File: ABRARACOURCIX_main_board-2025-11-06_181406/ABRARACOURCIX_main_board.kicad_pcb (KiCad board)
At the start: 2 copper layers, 140 x 140 mm, 72 parts, among them J1 Conn_01x02_Pin, J10 Conn_01x03_Socket, J11 Conn_01x03_Socket, J12 Conn_01x02_Pin, J2 XT60PW-M, J3 XT60PW-M, J4 Conn_01x06_Socket, J5 Conn_01x05_Socket, J6 Conn_01x03_Socket, J7 XT60PW-F, J8 Conn_01x03_Socket, J9 Conn_01x03_Socket, K1 Relai_T9GV1L14-5, Q2 NTR4101PT1G, Q3 MMBT3904, U2 Current_sens_ACS712ELCTR-20A-T, U3 AZ1117CH-3.3TRG1, U5 BNO055, U6 LMC6482, U7 LMC6482, U9 STM32F429VETx, Y2 ABS07-32.768KHZ-T

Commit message: Placement des composantes 95%
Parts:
- removed BUZ_D2: BAT54T1G, Diode_SMD:D_SOD-123
- removed BUZ_R3: 1k5, Resistor_SMD:R_1206_3216Metric_Pad1.30x1.75mm_HandSolder
- removed C12, C8, C9: 100n, Capacitor_SMD:C_1206_3216Metric_Pad1.33x1.80mm_HandSolder
- removed K1: Relai_T9GV1L14-5, Librairie_footprint:Relai_30A_T9GV1L14-5_TEC
- removed U9: STM32F429VETx, Package_QFP:LQFP-100_14x14mm_P0.5mm
- added Q5: DSS20200L-7-PNP, Package_TO_SOT_SMD:SOT-23-3, F.Cu at (-32.9, 6.80)
- added Q6: IKD15N60R, Package_TO_SOT_SMD:TO-252-2, F.Cu at (-45.1, 9.53)
- added R18: 1k5, Resistor_SMD:R_1206_3216Metric_Pad1.30x1.75mm_HandSolder, F.Cu at (-26.5, 12.0)
- added R19: 10k, Resistor_SMD:R_1206_3216Metric_Pad1.30x1.75mm_HandSolder, F.Cu at (-32.9, 2.20)
- added R2: 10k, Resistor_SMD:R_1206_3216Metric_Pad1.30x1.75mm_HandSolder, F.Cu at (-32.9, 12.0)
- added R20: 1k5, Resistor_SMD:R_1206_3216Metric_Pad1.30x1.75mm_HandSolder, F.Cu at (-26.5, 2.20)
- added U1: STM32F429VITx, Package_QFP:LQFP-100_14x14mm_P0.5mm, F.Cu at (13.5, -4.08)
- C27: footprint Capacitor_SMD:C_1206_3216Metric_Pad1.33x1.80mm_HandSolder -> Librairie_footprint:R60-CC_KEM
- Q3: value MMBT3904 -> NPN-DSS20201L-7; footprint Package_TO_SOT_SMD:SOT-23-3 -> Package_TO_SOT_SMD:SOT-23
- moved C27 187.4 mm to (-11.6, 32.9)
- moved C28 173.4 mm to (-39.2, 2.70)
- moved C29 173.1 mm to (-39.2, -1.10)
- moved DZ1 164.0 mm to (-29.2, -9.15)
- moved C19 161.8 mm to (-1.60, 6.40), turned to 90 degrees
- moved D2 157.0 mm to (6.35, 20.1), turned to -90 degrees
- moved C3 155.6 mm to (-20.2, 9.93), turned to -90 degrees
- moved J1 154.7 mm to (-21.9, -9.95)
- moved R17 153.4 mm to (10.8, 20.0), turned to -90 degrees
- moved J12 149.0 mm to (0.00, -61.0), turned to 90 degrees
- moved C4 148.3 mm to (5.70, -14.7)
- moved C5 145.6 mm to (2.20, 6.40), turned to 90 degrees
- moved TP6 143.9 mm to (46.2, -45.4)
- moved TP7 143.9 mm to (46.2, -41.3)
- moved C2 143.1 mm to (-6.80, 11.1), turned to 90 degrees
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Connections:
- J7 pad 1: GND -> Net-(J7-Pad1)
- J7 pad 2: VBAT -> Net-(U2-IP-)
- U2 pad 3: Net-(Q2-D) -> Net-(U2-IP-)
- U2 pad 4: Net-(Q2-D) -> Net-(U2-IP-)
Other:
- board text added: "3v3 Power"
- board text added: "5V GND"
- board text added: "Debug"
- board text added: "MTA Buck 5V In"
- board text added: "PWM 5V GND"

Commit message: Documentation de composantes
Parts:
- removed U6: LMC6482, Librairie_footprint:SOIC127P599X175-8N
- added GND1: TestPoint, TestPoint:TestPoint_THTPad_2.0x2.0mm_Drill1.0mm, F.Cu at (11.1, -36.3)
- added GND2: TestPoint, TestPoint:TestPoint_THTPad_2.0x2.0mm_Drill1.0mm, F.Cu at (15.8, 15.6)
- added U4: LMC6482AIMX/NOPB, Librairie_footprint:SOIC127P599X175-8N, F.Cu at (0.18, -44.8)
- C27: footprint Librairie_footprint:R60-CC_KEM -> Librairie_footprint:CAP_MU_15750_RUB-L
- R10: value 3K -> 1K
- R5: value 3K -> 1k
- U7: value LMC6482 -> LMC6482AIMX/NOPB
- moved C1 78.8 mm to (64.2, -8.40), turned to 90 degrees
- moved J12 78.4 mm to (58.1, -8.30), turned to 180 degrees
- moved SDA1 61.2 mm to (6.20, -25.8)
- moved RX1 60.6 mm to (25.8, 11.7)
- moved SCL1 55.3 mm to (11.1, -25.8)
- moved R5 55.3 mm to (13.0, -15.3)
- moved TX1 52.9 mm to (25.8, 7.50)
- moved R10 44.2 mm to (8.10, -19.7)
- moved C27 23.1 mm to (0.20, 13.0)
- moved J6 12.2 mm to (12.2, 56.0), turned to -90 degrees
- moved PWR_R5 11.9 mm to (-21.9, -4.60), turned to 0 degrees
- moved J10 8.89 mm to (2.64, 56.0)
- moved C3 8.67 mm to (-14.8, 3.14), turned to 90 degrees
- moved J2 7.40 mm to (-38.5, -9.20), turned to 180 degrees
- moved R8 3.67 mm to (-13.1, -11.3), turned to 0 degrees
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- renumbered TP6 to RX1, TP5 to SCL1, TP4 to SDA1, TP7 to TX1
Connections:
- net Net-(J2--) renamed /Power/20A_pre_switch
- J4 pad 2: +5V -> HC_RX
- J4 pad 3: GND -> HC_TX
- J4 pad 4: HC_TX -> GND
- J4 pad 5: HC_RX -> +5V
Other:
- board text added: "HC-05 Breakout"
- board text added: "Input 16v8 max"
- board text added: "Output to ESC"
- board text added: "PWM Moteur GND"
- board text added: "Projet ABRARACOURCIX V1 GAULxDesign IV 2025 Nathan Armishaw Étienne Bernier Marc-André Tremblay Rémi Plante Félix Dion"

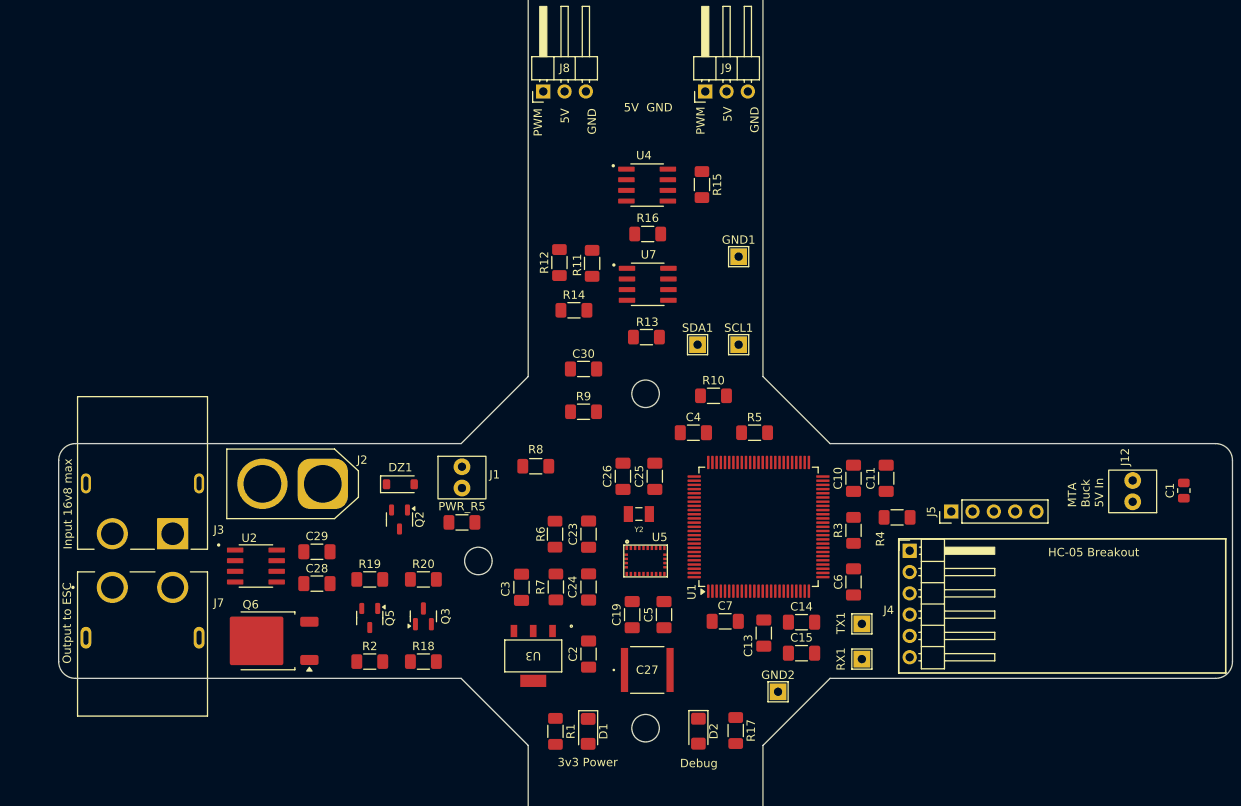
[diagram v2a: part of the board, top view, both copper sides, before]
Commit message: Déplacement des mounting holes et début du routing
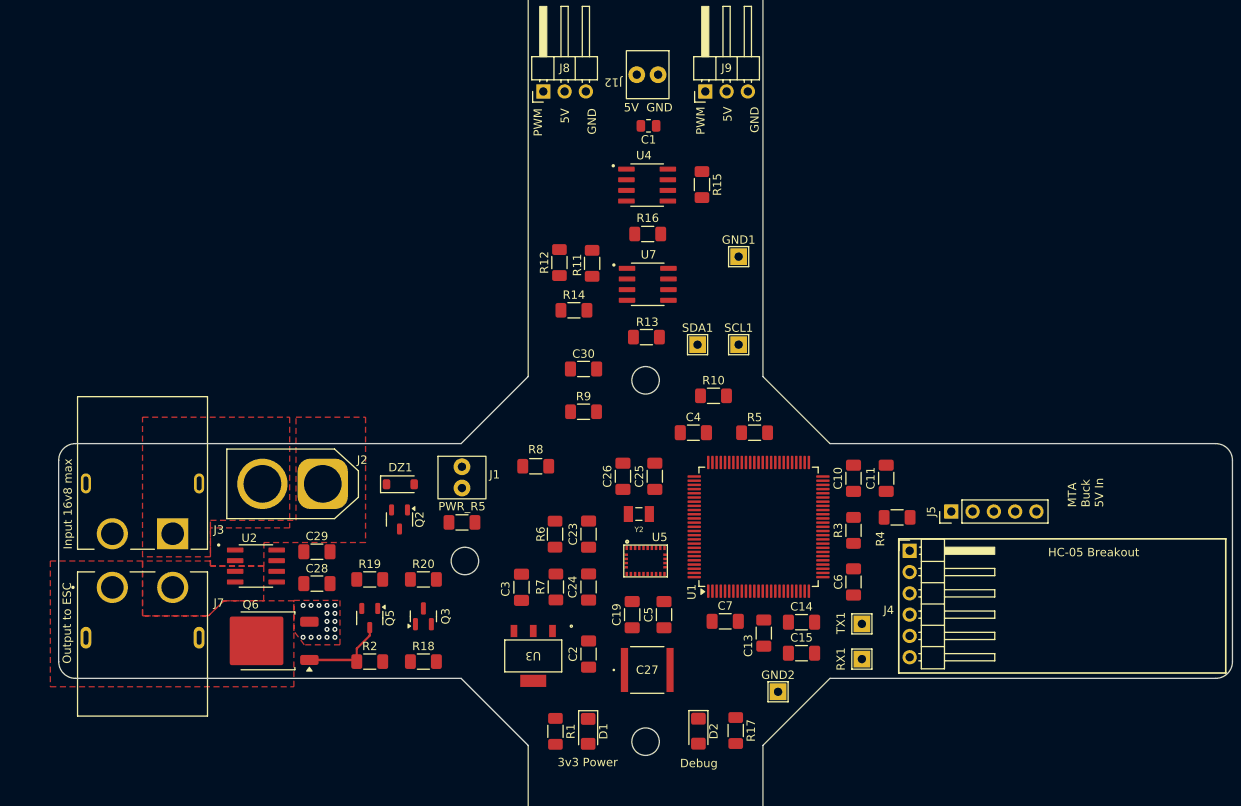
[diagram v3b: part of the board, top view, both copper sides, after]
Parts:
- moved C1 77.3 mm to (0.35, -51.9), turned to 180 degrees
- moved J12 76.3 mm to (0.25, -58.0), turned to -90 degrees
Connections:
- net /Power/20A_pre_switch renamed /Power/16V_pre-switch
- net Net-(J2-+) renamed /Power/16V_post-switch
- net Net-(J7-Pad1) renamed /Power/GND_IGBT
- net Net-(U2-IP-) renamed /Power/16V_motor
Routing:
- net Net-(Q5-PadC): track 0.00 -> 10.4 mm
- net GND: vias 0 -> 16
- added copper zone on F.Cu, net /Power/16V_motor
- added copper zone on F.Cu, net /Power/16V_post-switch
- added copper zone on F.Cu, net /Power/16V_pre-switch
- added copper zone on F.Cu, net /Power/GND_IGBT
- added copper zone on F.Cu, net GND
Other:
- outline, holes or cut-outs redrawn

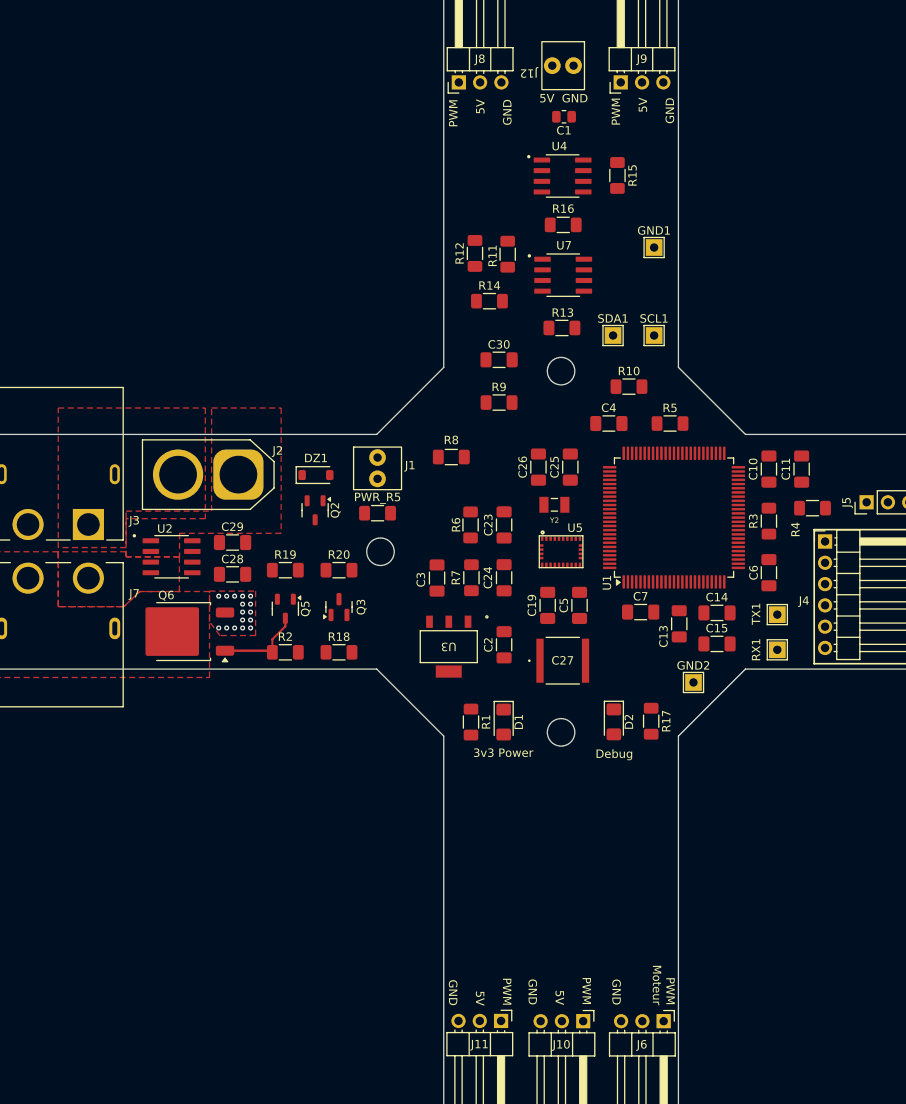
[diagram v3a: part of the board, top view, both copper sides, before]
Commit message: Avancement routing section power
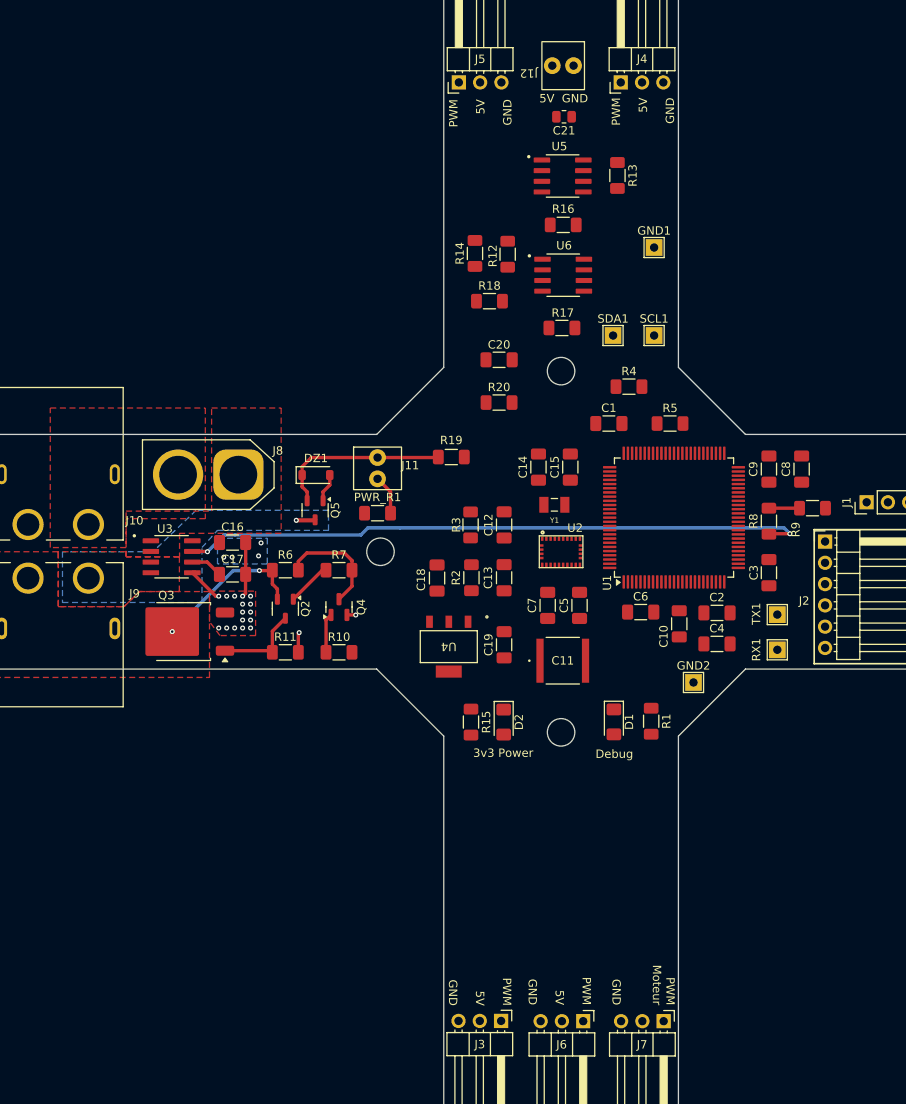
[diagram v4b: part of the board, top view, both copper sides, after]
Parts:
- renumbered C4 to C1, C13 to C10, C27 to C11, C23 to C12, C24 to C13, C26 to C14, C25 to C15, C29 to C16, C28 to C17, C3 to C18, C2 to C19, C14 to C2, C30 to C20, C1 to C21, C6 to C3, C15 to C4, C7 to C6, C19 to C7, C11 to C8, C10 to C9, D2 to D1, D1 to D2, J5 to J1, J3 to J10, J1 to J11, J4 to J2, J11 to J3, J9 to J4, J8 to J5, J10 to J6, J6 to J7, J2 to J8, J7 to J9, PWR_R5 to PWR_R1, Q5 to Q2, Q6 to Q3, Q3 to Q4, Q2 to Q5, R17 to R1, R18 to R10, R2 to R11, R11 to R12, R15 to R13, R12 to R14, R1 to R15, R13 to R17, R14 to R18, R8 to R19, R7 to R2, R9 to R20, R6 to R3, R10 to R4, R19 to R6, R20 to R7, R3 to R8, R4 to R9, U5 to U2, U2 to U3, U3 to U4, U4 to U5, U7 to U6, Y2 to Y1
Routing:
- net Net-(U3-VIOUT): track 0.00 -> 75.3 mm, vias 0 -> 2
- net VBAT_sense: track 0.00 -> 21.0 mm
- net GND: track 0.00 -> 19.4 mm, vias 16 -> 18
- net /Power/GND_IGBT: track 0.00 -> 18.7 mm, vias 0 -> 2
- net Net-(Q4-PadC): track 0.00 -> 13.5 mm
- net Net-(Q2-PadB): track 0.00 -> 5.33 mm
- net Net-(Q4-PadB): track 0.00 -> 4.71 mm
- net Net-(U3-FILTER): track 0.00 -> 3.84 mm
- net VIout_sense: track 0.00 -> 3.65 mm
- net Net-(DZ1-A): track 0.00 -> 3.39 mm
- net /Power/16V_motor: track 0.00 -> 2.29 mm, vias 0 -> 1
- net +5V: vias 0 -> 4
- added copper zone on B.Cu, net +5V
- added copper zone on B.Cu, net /Power/16V_motor

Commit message: Routing terminé (v1)
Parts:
- moved C11 58.6 mm to (-9.50, -44.8), turned to 180 degrees
- moved C8 22.4 mm to (7.05, -15.6), turned to -90 degrees
- moved RX1 4.35 mm to (24.9, 7.45)
- moved TX1 4.16 mm to (24.9, 11.6)
- moved C1 2.11 mm to (3.60, -15.6), turned to 90 degrees
- moved C7 0.96 mm to (-1.60, 7.36)
- moved C5 0.94 mm to (2.25, 7.34)
- moved C21 0.45 mm to (0.30, -52.4)
- turned C15 to -90 degrees
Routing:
- net GND: track 19.4 -> 116.4 mm, vias 18 -> 42
- net PWM_Servo_4: track 0.00 -> 76.5 mm, vias 0 -> 5
- net PWM_Servo_1: track 0.00 -> 73.1 mm, vias 0 -> 5
- net PWM_Moteur: track 0.00 -> 71.4 mm, vias 0 -> 7
- net PWM_Servo_2: track 0.00 -> 60.9 mm, vias 0 -> 3
- net Motor_switch: track 0.00 -> 53.4 mm, vias 0 -> 7
- net PWM_Servo_3: track 0.00 -> 49.5 mm, vias 0 -> 1
- net VBAT_ADC: track 0.00 -> 49.5 mm, vias 0 -> 2
- net HC_TX: track 0.00 -> 39.3 mm, vias 0 -> 1
- net HC_RX: track 0.00 -> 36.6 mm, vias 0 -> 1
- net SYS_SWCLK: track 0.00 -> 36.0 mm, vias 0 -> 1
- net NRST: track 0.00 -> 35.5 mm, vias 0 -> 1
- net SCL: track 0.00 -> 33.1 mm, vias 0 -> 3
- net SDA: track 0.00 -> 32.3 mm, vias 0 -> 2
- net SYS_SWDIO: track 0.00 -> 30.5 mm, vias 0 -> 1
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- added copper zone on F.Cu, net +3.3V
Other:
- board text added: "Projet ABRARACOURCIX V1 GAULxDesign IV 2025 Nathan Armishaw Etienne Bernier Marc-André Tremblay Rémi Plante Félix Dion"
- board text removed: "Projet ABRARACOURCIX V1 GAULxDesign IV 2025 Nathan Armishaw Étienne Bernier Marc-André Tremblay Rémi Plante Félix Dion"

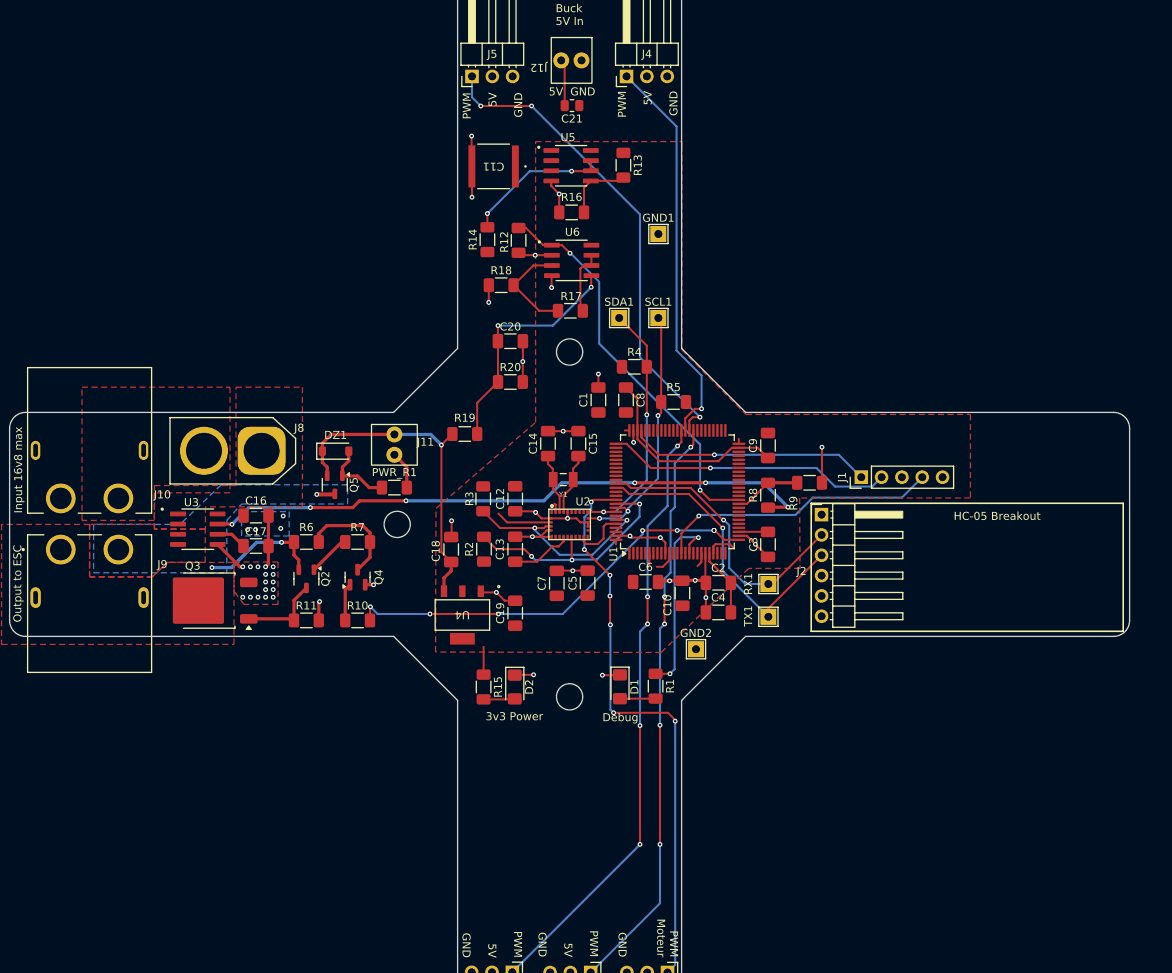
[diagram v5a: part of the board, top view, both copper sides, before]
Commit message: Ajout de dessins et info silkscreen
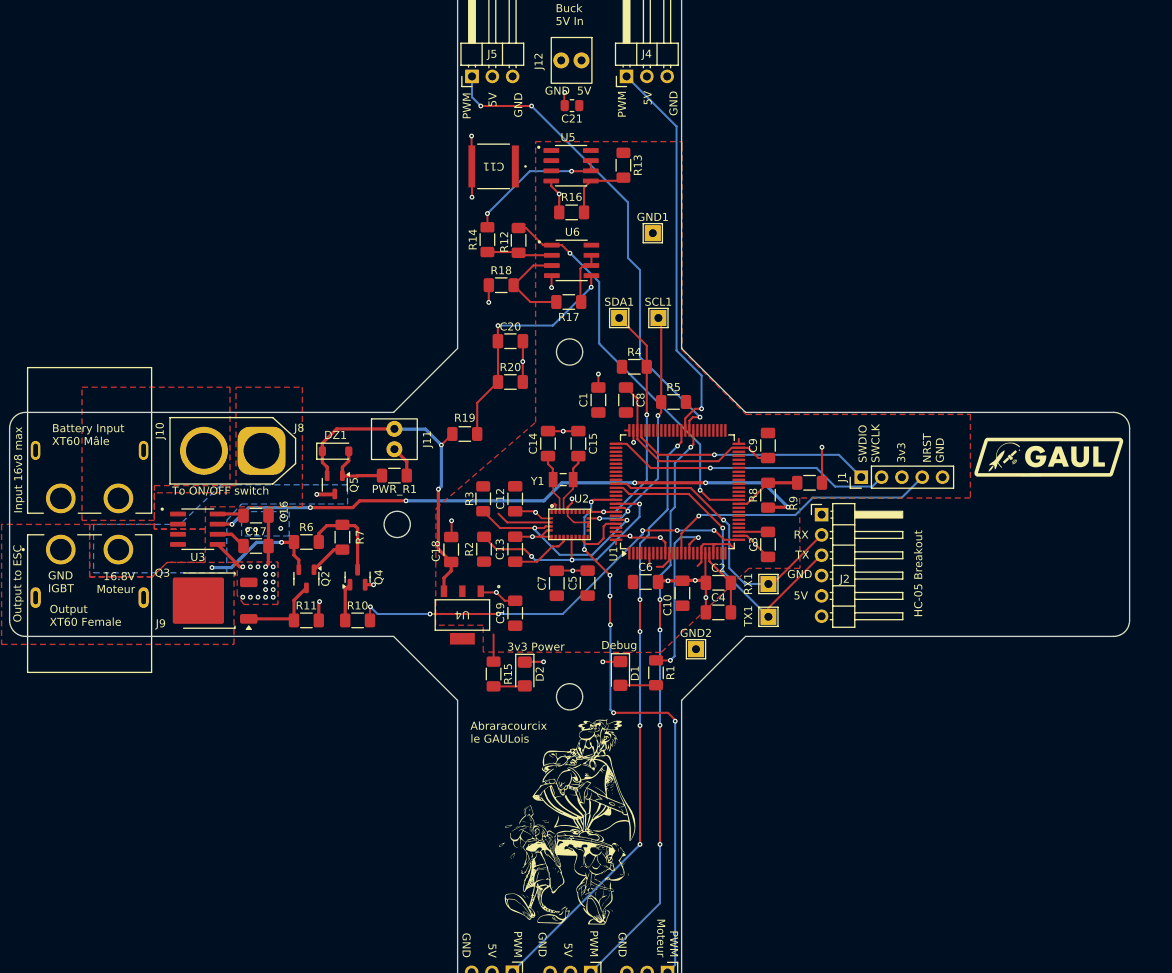
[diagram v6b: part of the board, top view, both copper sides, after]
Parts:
- added Abraracourcix_moyen: LOGO, Librairie_footprint:Abraracourcix_moyen, F.Cu at (0.00, 37.1)
- added G***: LOGO, Librairie_footprint:Abraracourcix_negatif, F.Cu at (0.00, 0.00)
- added G***2: LOGO, LOGO, F.Cu at (59.9, -8.40)
- added G***3: LOGO, LOGO, B.Cu at (52.9, 4.70)
- moved D2 2.05 mm to (-5.60, 18.7)
- moved R15 2.05 mm to (-9.50, 18.7)
- moved R7 1.99 mm to (-28.4, 1.60), turned to 90 degrees
- moved D1 1.67 mm to (6.35, 18.6)
- moved R1 1.67 mm to (10.8, 18.6)
- moved PWR_R1 1.50 mm to (-21.9, -6.10)
- moved R17 1.12 mm to (-0.10, -27.8)
- moved GND1 0.71 mm to (10.4, -36.4)
- moved J11 0.70 mm to (-21.9, -10.7)
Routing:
- net GND: track 116.4 -> 111.6 mm, vias 42 -> 43
- net Net-(U6A--): track 4.42 -> 8.23 mm, vias 1 -> 0
- net +5V: track 0.00 -> 3.32 mm
- net +3.3V: track 27.2 -> 30.1 mm
- net Net-(Q4-PadC): track 13.5 -> 11.6 mm
- net Net-(U1-PC1): track 24.3 -> 22.6 mm
- net Net-(U6B--): track 8.21 -> 7.02 mm
- net VBAT_sense: track 41.3 -> 42.2 mm, vias 1 -> 2
- net XOUT32: track 8.08 -> 8.88 mm
- net Net-(Q2-PadB): track 5.33 -> 4.59 mm
- net Net-(DZ1-A): track 8.96 -> 8.38 mm
- net Net-(U6A-+): track 12.7 -> 12.1 mm
- net Motor_switch: vias 7 -> 6
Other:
- board text added: "16.8V"
- board text added: "16.8V Moteur"
- board text added: "5V"
- board text added: "Abraracourcix le GAULois"
- board text added: "Battery Input"
- board text added: "Battery Input XT60 Mâle"
- board text added: "GND"
- board text added: "GND 5V"
- board text added: "GND IGBT"
- board text added: "Output XT60 Female"
- board text added: "Projet ABRARACOURCIX: Asservissement en Boucles et Régulation Avancée RApide pour le Contrôle d'Objet Unirotorisé Réactifs avec Capteur Inertiel eXpérimental"
- board text added: "RX"
- board text added: "SCL"
- board text added: "SDA"
- board text added: "SWDIO SWCLK 3v3 NRST GND"
- board text added: "TX"
- board text added: "To ON/OFF switch"
